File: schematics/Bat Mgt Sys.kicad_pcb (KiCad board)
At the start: 4 copper layers, 121 x 78 mm, 63 parts, among them J1 USB_C_Receptacle_PowerOnly_6P, J2 USB_A, J3 Screw_Terminal_01x02, J4 Screw_Terminal_01x02, Q1 IRLML6402, Q2 IRLML6402, U1 TPD1E05U06DPY, U2 TPD1E05U06DPY, U3 TPS2592xx, U4 TLV76701DRVx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

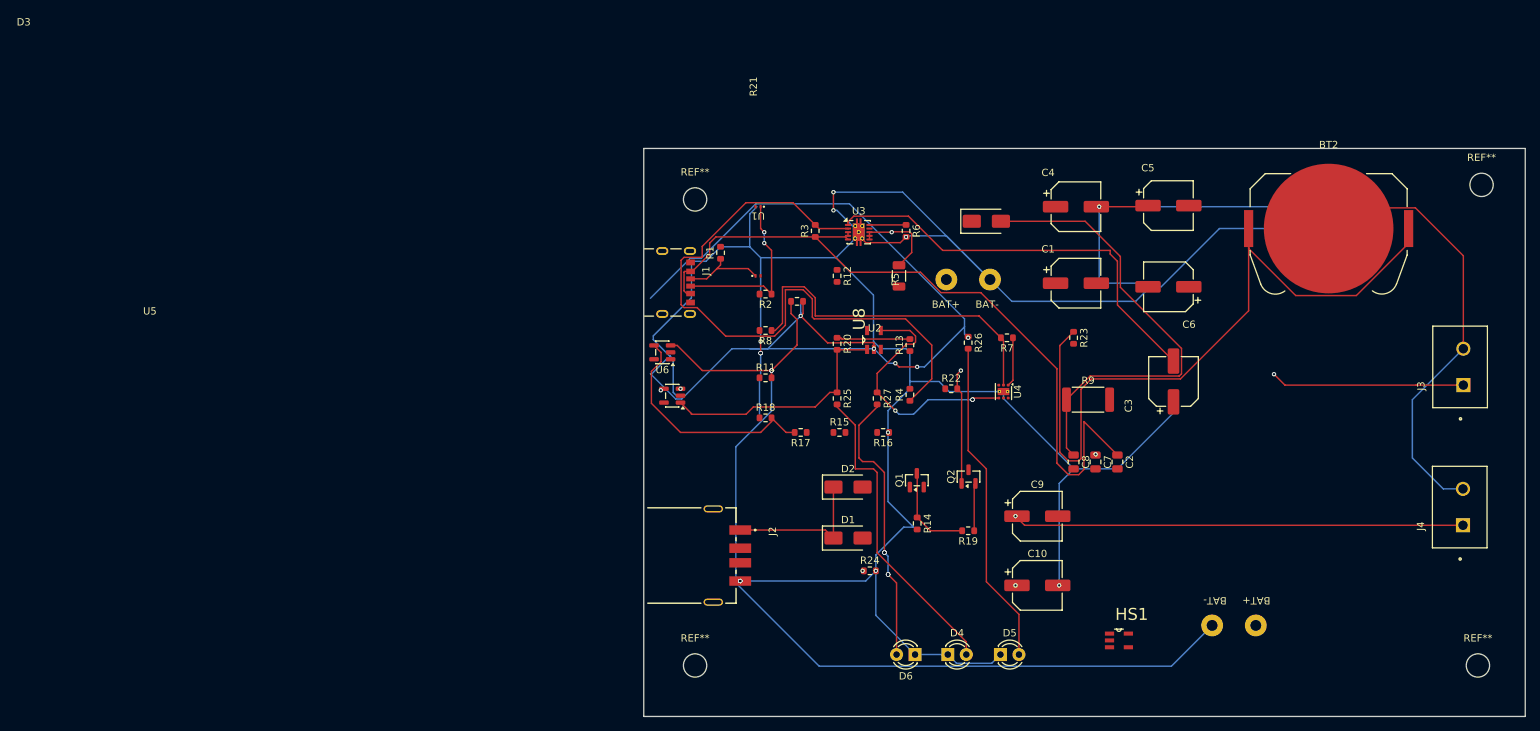
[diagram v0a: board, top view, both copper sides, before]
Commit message: updated simulation parameters, and adjusted file locations
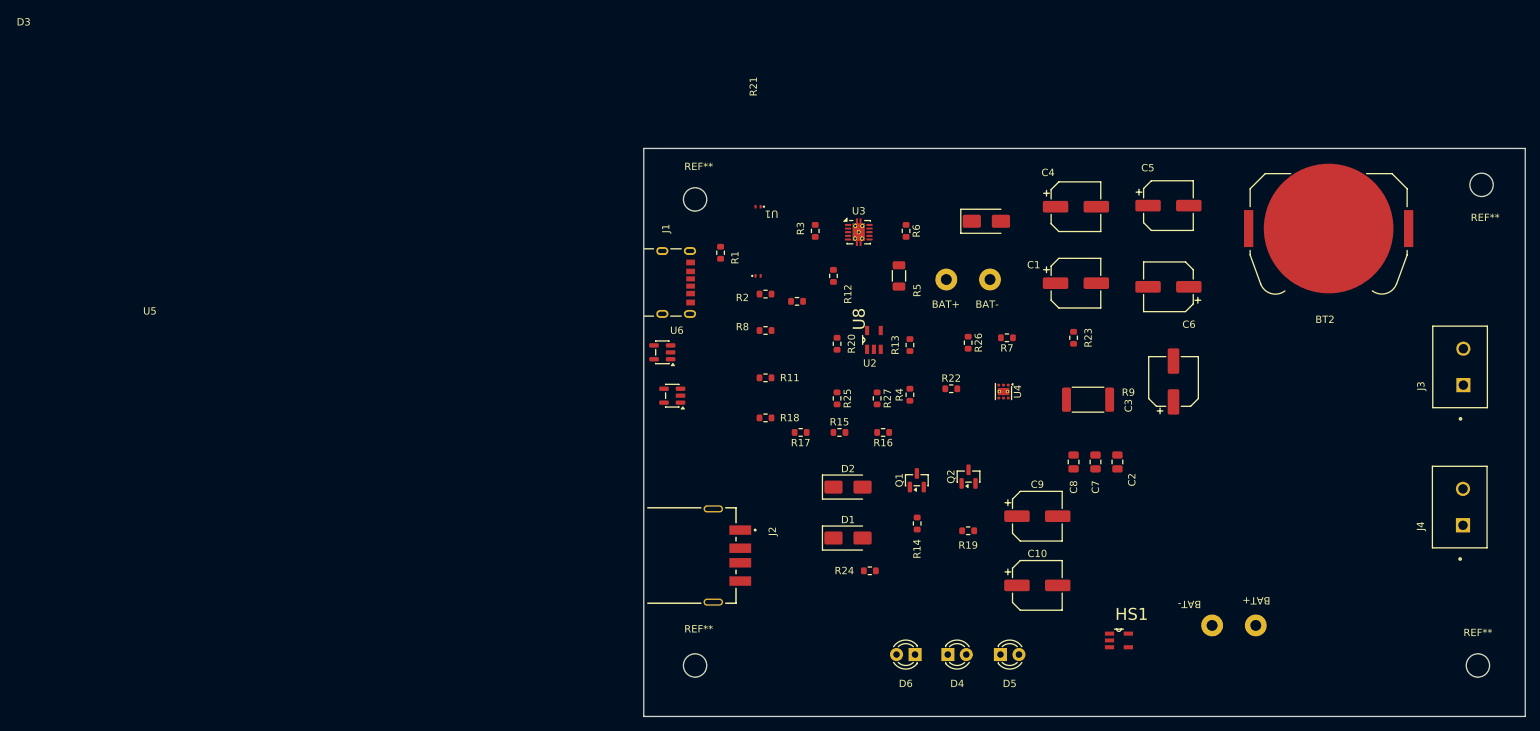
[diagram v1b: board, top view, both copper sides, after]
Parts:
- moved R12 0.50 mm to (91.0, 65.5)
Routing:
- net GND: track 462.1 -> 0.00 mm, vias 14 -> 0
- net +POUT: track 251.2 -> 0.00 mm, vias 2 -> 0
- net /VOUT: track 138.1 -> 0.00 mm, vias 1 -> 0
- net /TH_OUT: track 138.1 -> 0.00 mm, vias 5 -> 0
- net Net-(U6-+): track 131.2 -> 0.00 mm, vias 2 -> 0
- net Net-(BT2-+): track 101.5 -> 0.00 mm
- net /IN: track 101.1 -> 0.00 mm
- net +BOUT: track 94.8 -> 0.00 mm, vias 2 -> 0
- net Net-(U3-EN/UVLO): track 89.9 -> 0.00 mm
- net /V_REF+: track 67.0 -> 0.00 mm, vias 1 -> 0
- net Net-(D3-A): track 63.3 -> 0.00 mm
- net Net-(U3-dV/dT): track 57.5 -> 0.00 mm
- net +BAT: track 54.6 -> 0.00 mm
- net Net-(U4-FB): track 47.9 -> 0.00 mm
- net Net-(D5-A): track 44.9 -> 0.00 mm
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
